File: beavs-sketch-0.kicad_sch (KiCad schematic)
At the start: 28 parts, among them J1 USB_C_Receptacle_USB2.0_16P, J13 USB_C_Receptacle_USB2.0_16P, J3 Conn_01x02, J5 Conn_01x02, Q2 SiS427EDN, U15 SN74LVC8T245, U16 SRV05-4, U17 SRV05-4, U7 AMS1117-3.3, U8 AMS1117-5.0

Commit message: change out LEDs, add silk, start getting ready for fab
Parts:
- removed J13: USB_C_Receptacle_USB2.0_16P, Connector_USB:USB_C_Receptacle_G-Switch_GT-USB-7051x, symbol Connector:USB_C_Receptacle_USB2.0_16P
- D1, D2, D3, D4, D5, D6: value WS2812B-2020 -> SK6812-EC20; footprint LED_SMD:LED_WS2812B-2020_PLCC4_2.0x2.0mm -> beavs-footprints:LED_SK6812-EC20_PLCC4_2.0x2.0mm; symbol LED:WS2812B-2020 -> beavs-symbols:SK6812-EC20
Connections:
- net +5V: now also D1.1 (VDD), D2.1 (VDD), D3.1 (VDD), D4.1 (VDD), D5.1 (VDD), D6.1 (VDD); no longer D1.4 (VDD), D2.4 (VDD), D3.4 (VDD), D4.4 (VDD), D5.4 (VDD), D6.4 (VDD)
- net GND: now also D1.3 (VSS), D2.3 (VSS), D3.3 (VSS), D4.3 (VSS), D5.3 (VSS), D6.3 (VSS); no longer D1.2 (VSS), D2.2 (VSS), D3.2 (VSS), D4.2 (VSS), D5.2 (VSS), D6.2 (VSS)
- net at U15.15 (B7): now also D1.4 (DIN); no longer D1.3 (DIN)
- new net: D4.2 (DOUT), D5.4 (DIN)
- new net: D3.2 (DOUT), D4.4 (DIN)
- new net: D5.2 (DOUT), D6.4 (DIN)
- new net: D2.2 (DOUT), D3.4 (DIN)
- new net: D1.2 (DOUT), D2.4 (DIN)
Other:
- sheet Sensors ports: added EXTINT; removed none
- sheet mcu ports: added GPIO_EXTINT; removed none
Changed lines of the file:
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@@
 	)
 	(junction
-		(at 185.42 77.47)
+		(at 185.42 81.28)
 		(diameter 0)
 		(color 0 0 0 0)
@@
 	)
 	(junction
-		(at 187.96 74.93)
+		(at 187.96 78.74)
 		(diameter 0)
 		(color 0 0 0 0)
@@
 	(wire
 		(pts
-			(xy 185.42 77.47) (xy 190.5 77.47)
+			(xy 185.42 81.28) (xy 190.5 81.28)
 		)
 		(stroke
@@
 	(wire
 		(pts
-			(xy 187.96 95.25) (xy 187.96 74.93)
+			(xy 187.96 95.25) (xy 187.96 78.74)
 		)
 		(stroke
@@
 	(wire
 		(pts
-			(xy 185.42 77.47) (xy 185.42 97.79)
+			(xy 185.42 81.28) (xy 185.42 97.79)
 		)
 		(stroke
@@
 	(wire
 		(pts
-			(xy 176.53 74.93) (xy 187.96 74.93)
+			(xy 176.53 78.74) (xy 187.96 78.74)
 		)
 		(stroke
@@
 	(wire
 		(pts
+			(xy 176.53 74.93) (xy 190.5 74.93)
+		)
+		(stroke
+			(width 0)
+			(type default)
+		)
+	)
+	(wire
+		(pts
 			(xy 207.01 142.24) (xy 273.05 142.24)
 		)
@@
 	(wire
 		(pts
-			(xy 187.96 74.93) (xy 190.5 74.93)
+			(xy 187.96 78.74) (xy 190.5 78.74)
 		)
 		(stroke
@@
 	(wire
 		(pts
-			(xy 176.53 77.47) (xy 185.42 77.47)
+			(xy 176.53 81.28) (xy 185.42 81.28)
 		)
 		(stroke
@@
 	)
 	(symbol
-		(lib_id "LED:WS2812B-2020")
+		(lib_id "beavs-symbols:SK6812-EC20")
 		(at 302.26 172.72 0)
 		(unit 1)
@@
 			)
 		)
-		(property "Value" "WS2812B-2020"
+		(property "Value" "SK6812-EC20"
 			(at 316.23 168.8398 0)
 			(effects
@@
 			)
 		)
-		(property "Footprint" "LED_SMD:LED_WS2812B-2020_PLCC4_2.0x2.0mm"
+		(property "Footprint" "beavs-footprints:LED_SK6812-EC20_PLCC4_2.0x2.0mm"
 			(at 303.53 180.34 0)
 			(effects
@@
 			)
 		)
-		(property "Description" "RGB LED with integrated controller, 2.0 x 2.0 mm, 12 mA"
+		(property "Description" "RGB LED with integrated controller"
 			(at 302.26 172.72 0)
 			(effects
@@
 	)
 	(symbol
-		(lib_id "LED:WS2812B-2020")
+		(lib_id "beavs-symbols:SK6812-EC20")
 		(at 318.77 172.72 0)
 		(unit 1)
@@
 			)
 		)
-		(property "Value" "WS2812B-2020"
+		(property "Value" "SK6812-EC20"
 			(at 332.74 168.8398 0)
 			(effects
@@
 			)
 		)
-		(property "Footprint" "LED_SMD:LED_WS2812B-2020_PLCC4_2.0x2.0mm"
+		(property "Footprint" "beavs-footprints:LED_SK6812-EC20_PLCC4_2.0x2.0mm"
 			(at 320.04 180.34 0)
 			(effects
@@
 			)
 		)
-		(property "Description" "RGB LED with integrated controller, 2.0 x 2.0 mm, 12 mA"
+		(property "Description" "RGB LED with integrated controller"
 			(at 318.77 172.72 0)
 			(effects
@@
 	)
 	(symbol
-		(lib_id "LED:WS2812B-2020")
+		(lib_id "beavs-symbols:SK6812-EC20")
 		(at 269.24 172.72 0)
 		(unit 1)
@@
 			)
 		)
-		(property "Value" "WS2812B-2020"
+		(property "Value" "SK6812-EC20"
 			(at 283.21 168.8398 0)
 			(effects
@@
 			)
 		)
-		(property "Footprint" "LED_SMD:LED_WS2812B-2020_PLCC4_2.0x2.0mm"
+		(property "Footprint" "beavs-footprints:LED_SK6812-EC20_PLCC4_2.0x2.0mm"
 			(at 270.51 180.34 0)
 			(effects
@@
 			)
 		)
-		(property "Description" "RGB LED with integrated controller, 2.0 x 2.0 mm, 12 mA"
+		(property "Description" "RGB LED with integrated controller"
 			(at 269.24 172.72 0)
 			(effects
@@
 	)
 	(symbol
-		(lib_id "LED:WS2812B-2020")
+		(lib_id "beavs-symbols:SK6812-EC20")
 		(at 335.28 172.72 0)
 		(unit 1)
@@
 			)
 		)
-		(property "Value" "WS2812B-2020"
+		(property "Value" "SK6812-EC20"
 			(at 349.25 168.8398 0)
 			(effects
@@
 			)
 		)
-		(property "Footprint" "LED_SMD:LED_WS2812B-2020_PLCC4_2.0x2.0mm"
+		(property "Footprint" "beavs-footprints:LED_SK6812-EC20_PLCC4_2.0x2.0mm"
 			(at 336.55 180.34 0)
 			(effects
@@
 			)
 		)
-		(property "Description" "RGB LED with integrated controller, 2.0 x 2.0 mm, 12 mA"
+		(property "Description" "RGB LED with integrated controller"
 			(at 335.28 172.72 0)
 			(effects
@@
 	)
 	(symbol
-		(lib_id "Connector:USB_C_Receptacle_USB2.0_16P")
-		(at 20.32 83.82 0)
-		(unit 1)
-		(exclude_from_sim no)
-		(in_bom yes)
-		(on_board yes)
-		(dnp no)
-		(fields_autoplaced yes)
-		(property "Reference" "J13"
-			(at 20.32 60.96 0)
-			(effects
-				(font
-					(size 1.27 1.27)
-				)
-			)
-		)
-		(property "Value" "USB_C_Receptacle_USB2.0_16P"
-			(at 20.32 63.5 0)
-			(effects
-				(font
-					(size 1.27 1.27)
-				)
-			)
-		)
-		(property "Footprint" "Connector_USB:USB_C_Receptacle_G-Switch_GT-USB-7051x"
-			(at 24.13 83.82 0)
-			(effects
-				(font
-					(size 1.27 1.27)
-				)
-				(hide yes)
-			)
-		)
-		(property "Datasheet" "https://www.usb.org/sites/default/files/documents/usb_type-c.zip"
-			(at 24.13 83.82 0)
-			(effects
-				(font
-					(size 1.27 1.27)
-				)
-				(hide yes)
-			)
-		)
-		(property "Description" "USB 2.0-only 16P Type-C Receptacle connector"
-			(at 20.32 83.82 0)
-			(effects
-				(font
-					(size 1.27 1.27)
-				)
-				(hide yes)
-			)
-		)
-		(pin "A5"
-		)
-		(pin "B5"
-		)
-		(pin "B4"
-		)
-		(pin "B6"
-		)
-		(pin "A12"
-		)
-		(pin "A7"
-		)
-		(pin "S1"
-		)
-		(pin "A8"
-		)
-		(pin "B12"
-		)
-		(pin "A1"
-		)
-		(pin "B7"
-		)
-		(pin "B9"
-		)
-		(pin "B8"
-		)
-		(pin "B1"
-		)
-		(pin "A9"
-		)
-		(pin "A6"
-		)
-		(pin "A4"
-		)
-		(instances
-			(project ""
-				(path "/49232f62-a438-4b3e-9be5-c2b3074d8de1"
-					(reference "J13")
-					(unit 1)
-				)
-			)
-		)
-	)
-	(symbol
 		(lib_id "Device:R_Small")
 		(at 111.76 190.5 0)
@@
 	)
 	(symbol
-		(lib_id "LED:WS2812B-2020")
+		(lib_id "beavs-symbols:SK6812-EC20")
 		(at 252.73 172.72 0)
 		(unit 1)
@@
 			)
 		)
-		(property "Value" "WS2812B-2020"
+		(property "Value" "SK6812-EC20"
 			(at 266.7 168.8398 0)
 			(effects
@@
 			)
 		)
-		(property "Footprint" "LED_SMD:LED_WS2812B-2020_PLCC4_2.0x2.0mm"
+		(property "Footprint" "beavs-footprints:LED_SK6812-EC20_PLCC4_2.0x2.0mm"
 			(at 254 180.34 0)
 			(effects
@@
 			)
 		)
-		(property "Description" "RGB LED with integrated controller, 2.0 x 2.0 mm, 12 mA"
+		(property "Description" "RGB LED with integrated controller"
 			(at 252.73 172.72 0)
 			(effects
@@
 	)
 	(symbol
-		(lib_id "LED:WS2812B-2020")
+		(lib_id "beavs-symbols:SK6812-EC20")
 		(at 285.75 172.72 0)
 		(unit 1)
@@
 			)
 		)
-		(property "Value" "WS2812B-2020"
+		(property "Value" "SK6812-EC20"
 			(at 299.72 168.8398 0)
 			(effects
@@
 			)
 		)
-		(property "Footprint" "LED_SMD:LED_WS2812B-2020_PLCC4_2.0x2.0mm"
+		(property "Footprint" "beavs-footprints:LED_SK6812-EC20_PLCC4_2.0x2.0mm"
 			(at 287.02 180.34 0)
 			(effects
@@
 			)
 		)
-		(property "Description" "RGB LED with integrated controller, 2.0 x 2.0 mm, 12 mA"
+		(property "Description" "RGB LED with integrated controller"
 			(at 285.75 172.72 0)
 			(effects
@@
 		)
 		(pin "SCL" output
-			(at 176.53 77.47 0)
+			(at 176.53 81.28 0)
 			(effects
 				(font
@@
 		)
 		(pin "SDA" bidirectional
-			(at 176.53 74.93 0)
+			(at 176.53 78.74 0)
 			(effects
 				(font
@@
 			)
 		)
+		(pin "GPIO_EXTINT" output
+			(at 176.53 74.93 0)
+			(effects
+				(font
+					(size 1.27 1.27)
+				)
+				(justify right)
+			)
+		)
 		(instances
 			(project "beavs-sketch-0"
@@
 		)
 		(pin "SCL" input
-			(at 190.5 77.47 180)
+			(at 190.5 81.28 180)
 			(effects
 				(font
@@
 		)
 		(pin "SDA" bidirectional
+			(at 190.5 78.74 180)
+			(effects
+				(font
+					(size 1.27 1.27)
+				)
+				(justify left)
+			)
+		)
+		(pin "EXTINT" input
 			(at 190.5 74.93 180)
 			(effects

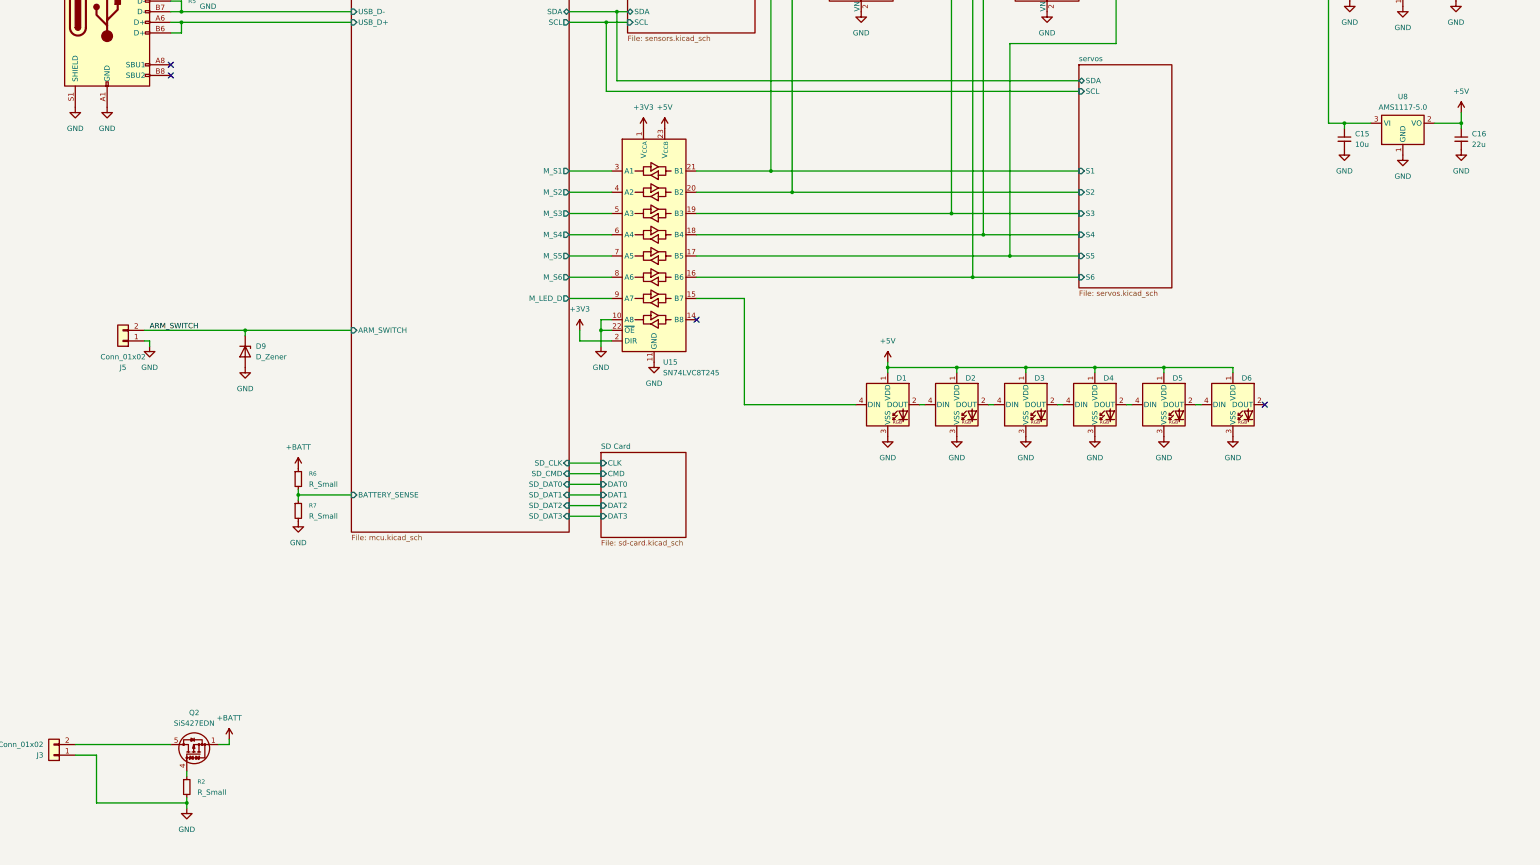
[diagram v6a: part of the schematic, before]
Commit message: stapling vias, silk, minor schematic tweaks
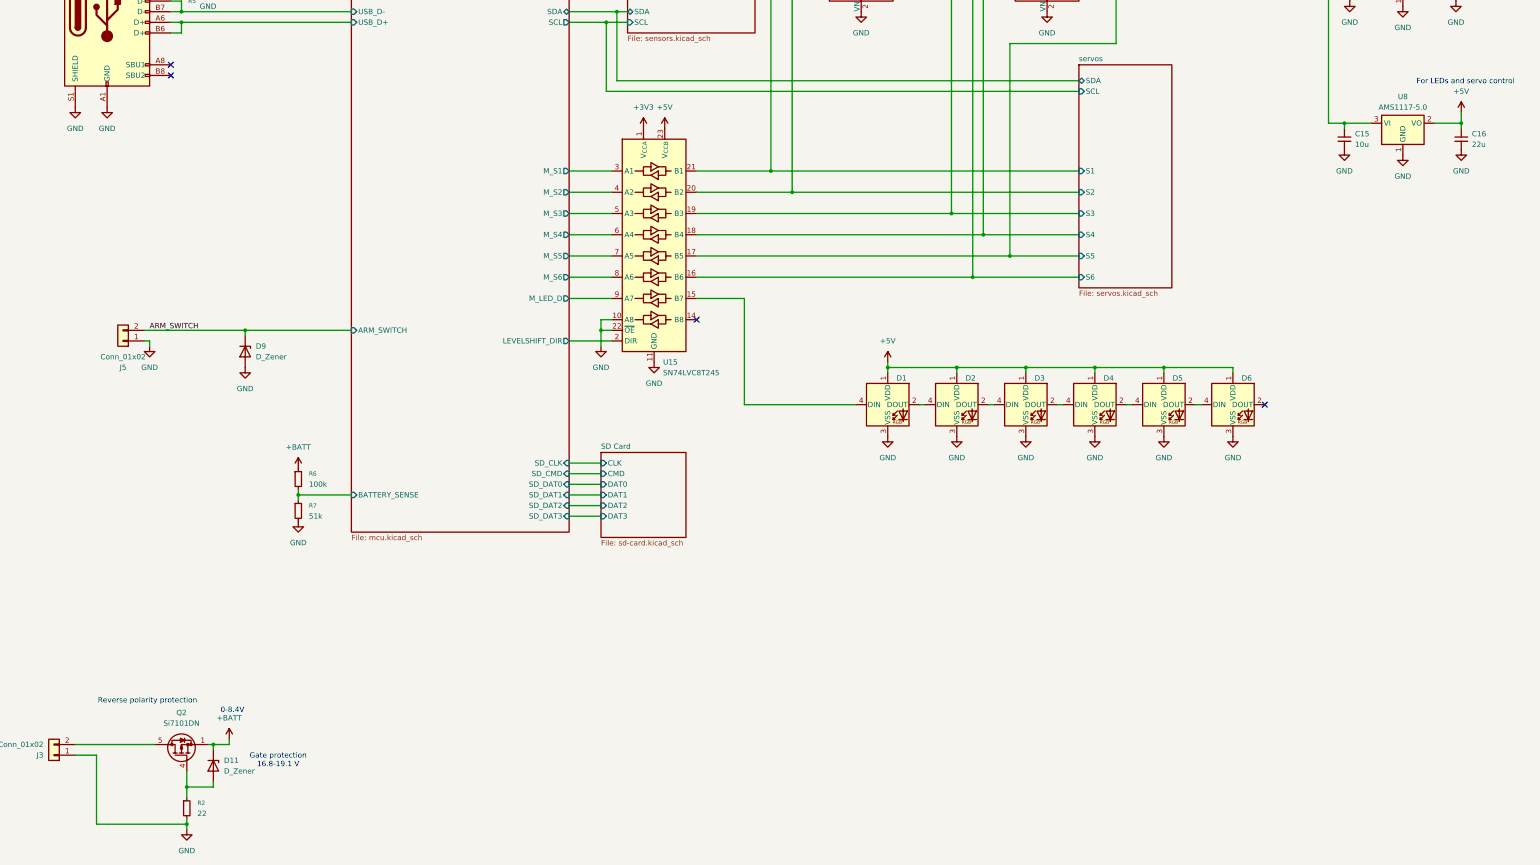
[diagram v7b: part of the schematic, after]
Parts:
- removed Q2: SiS427EDN, Package_SO:Vishay_PowerPAK_1212-8_Single, symbol beavs-symbols:SiS427EDN
- added D11: D_Zener, Diode_SMD:D_SOD-523, symbol Device:D_Zener
- added Q2: Si7101DN, Package_SO:Vishay_PowerPAK_1212-8_Single, symbol beavs-symbols:Si7101DN
- D1, D2, D3, D4, D5, D6: LCSC (none) -> C2909058
- R2: value R_Small -> 22; LCSC (none) -> C25092
- R6: value R_Small -> 100k; LCSC (none) -> C25741
- R7: value R_Small -> 51k; LCSC (none) -> C25794
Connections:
- net +3V3: no longer U15.2 (DIR)
- net +BATT: now also D11.1 (K), Q2.1 (S), Q2.2 (S), Q2.3 (S)
- net at J3.2 (Pin_2): now also Q2.5 (D)
- net at R2.1: now also D11.2 (A), Q2.4 (G)
- new net mcu/LEVELSHIFT_DIR: U15.2 (DIR)
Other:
- sheet mcu ports: added LEVELSHIFT_DIR; removed none
- note added: "0-8.4V"
- note added: "For LEDs and servo control"
- note added: "Gate protection 16.8-19.1 V"
- note added: "Reverse polarity protection"
- moved on the sheet: R2

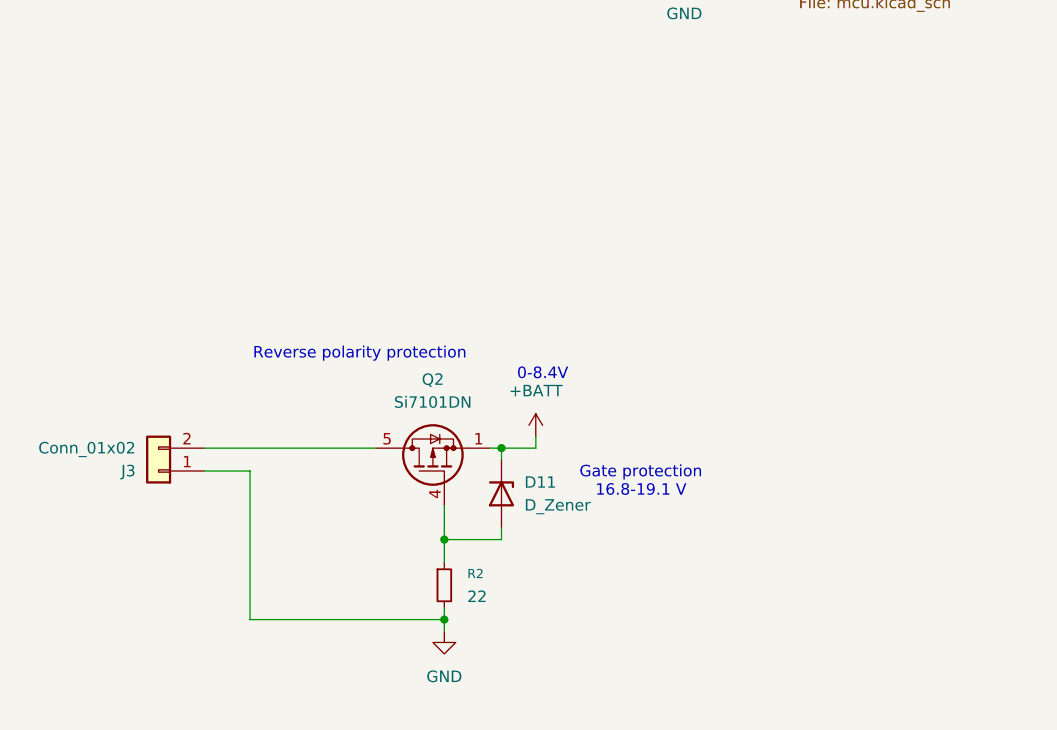
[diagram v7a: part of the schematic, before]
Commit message: moved to ideal diode + back to back FETs
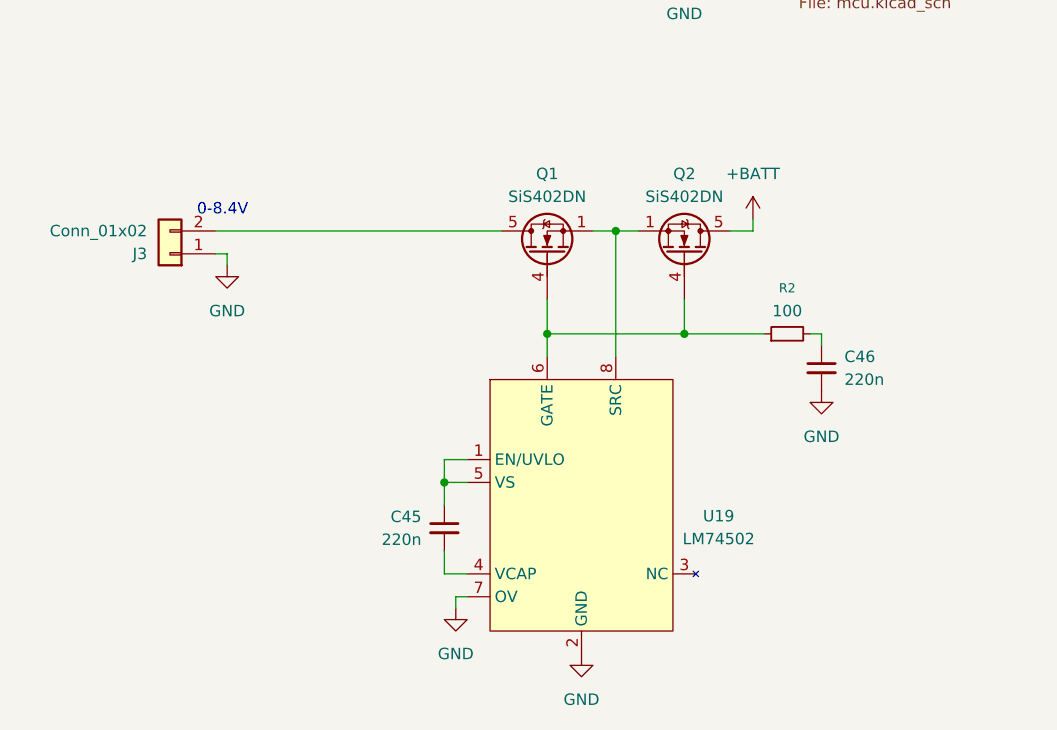
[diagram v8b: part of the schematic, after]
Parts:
- removed D11: D_Zener, Diode_SMD:D_SOD-523, symbol Device:D_Zener
- removed Q2: Si7101DN, Package_SO:Vishay_PowerPAK_1212-8_Single, symbol beavs-symbols:Si7101DN
- added C45, C46: 220n, Capacitor_SMD:C_0402_1005Metric, symbol Device:C_Small
- added Q1, Q2: SiS402DN, Package_SO:Vishay_PowerPAK_1212-8_Single, symbol Transistor_FET:Q_NMOS_SSSGD_AvalancheRated
- added U19: LM74502, Package_TO_SOT_SMD:SOT-23-8, symbol beavs-symbols:LM74502
- R2: value 22 -> 100; LCSC C25092 -> C25076
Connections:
- net +BATT: now also Q2.5 (D)
- net GND: now also C46.2, U19.2 (GND), U19.7 (OV); no longer R2.2
- net at R2.1: now also Q1.4 (G), Q2.4 (G), U19.6 (GATE)
- net at J3.2 (Pin_2): now also Q1.5 (D)
- new net: C46.1, R2.2
- new net: C45.1, U19.1 (EN/UVLO), U19.5 (VS)
- new net: C45.2, U19.4 (VCAP)
- new net: Q1.1 (S), Q1.2 (S), Q1.3 (S), Q2.1 (S), Q2.2 (S), Q2.3 (S), U19.8 (SRC)
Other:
- note removed: "Gate protection 16.8-19.1 V"
- note removed: "Reverse polarity protection"
- moved on the sheet: J3
